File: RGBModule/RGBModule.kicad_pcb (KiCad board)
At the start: 2 copper layers, 17.8 x 24.4 mm, 8 parts, among them P1 CONN_01X04

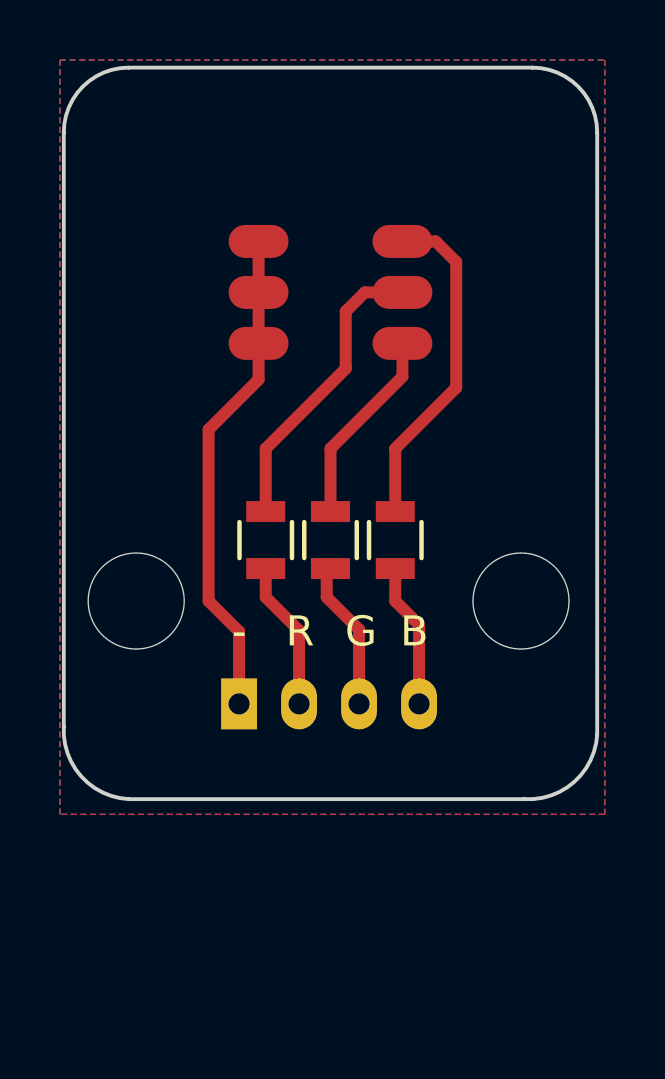
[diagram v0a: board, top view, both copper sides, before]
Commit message: Logo y conector cambiado
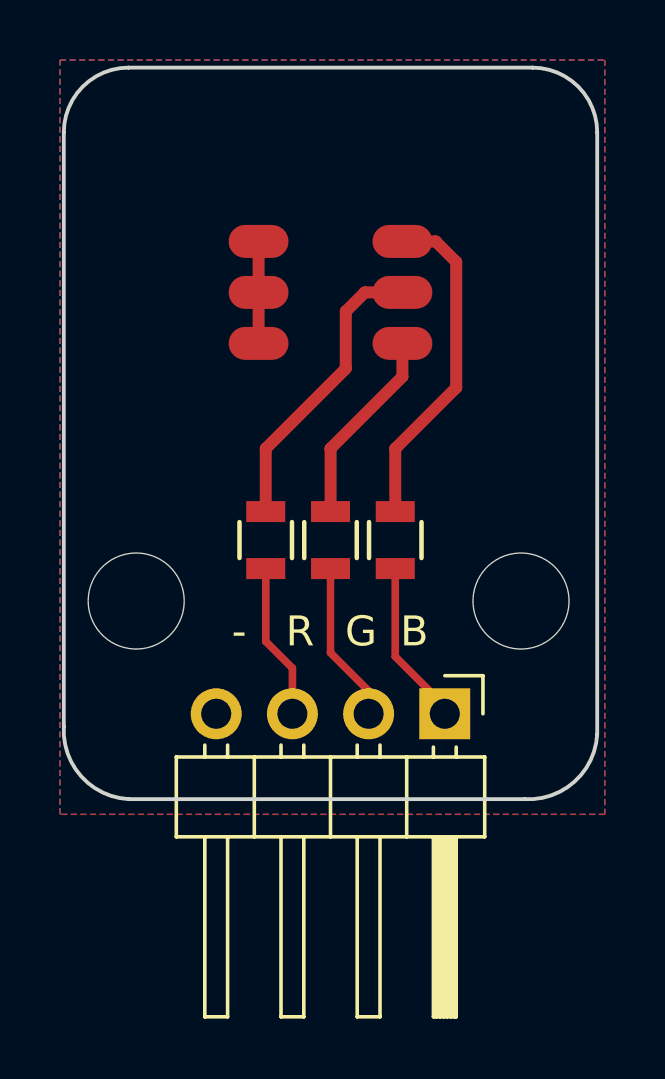
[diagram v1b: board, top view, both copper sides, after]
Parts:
- removed the G*** at (137.8, 98.4)
- added G***: LOGO, Grape:atom_medium, B.Cu at (137.9, 97.7)
- added G***: LOGO, logos_frizzy:web, B.Cu at (137.9, 104.6)
- P1: footprint Connectors_JST:JST_PH_S4B-PH-K_04x2.00mm_Angled -> Pin_Headers:Pin_Header_Angled_1x04_Pitch2.54mm
- moved P1 6.87 mm to (141.7, 111.7), turned to 270 degrees
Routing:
- net GND: track 16.5 -> 3.40 mm
- net BLUE: track 4.84 -> 5.53 mm
- net GREEN: track 5.01 -> 5.55 mm
